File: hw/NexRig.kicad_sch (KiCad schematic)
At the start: 7 parts

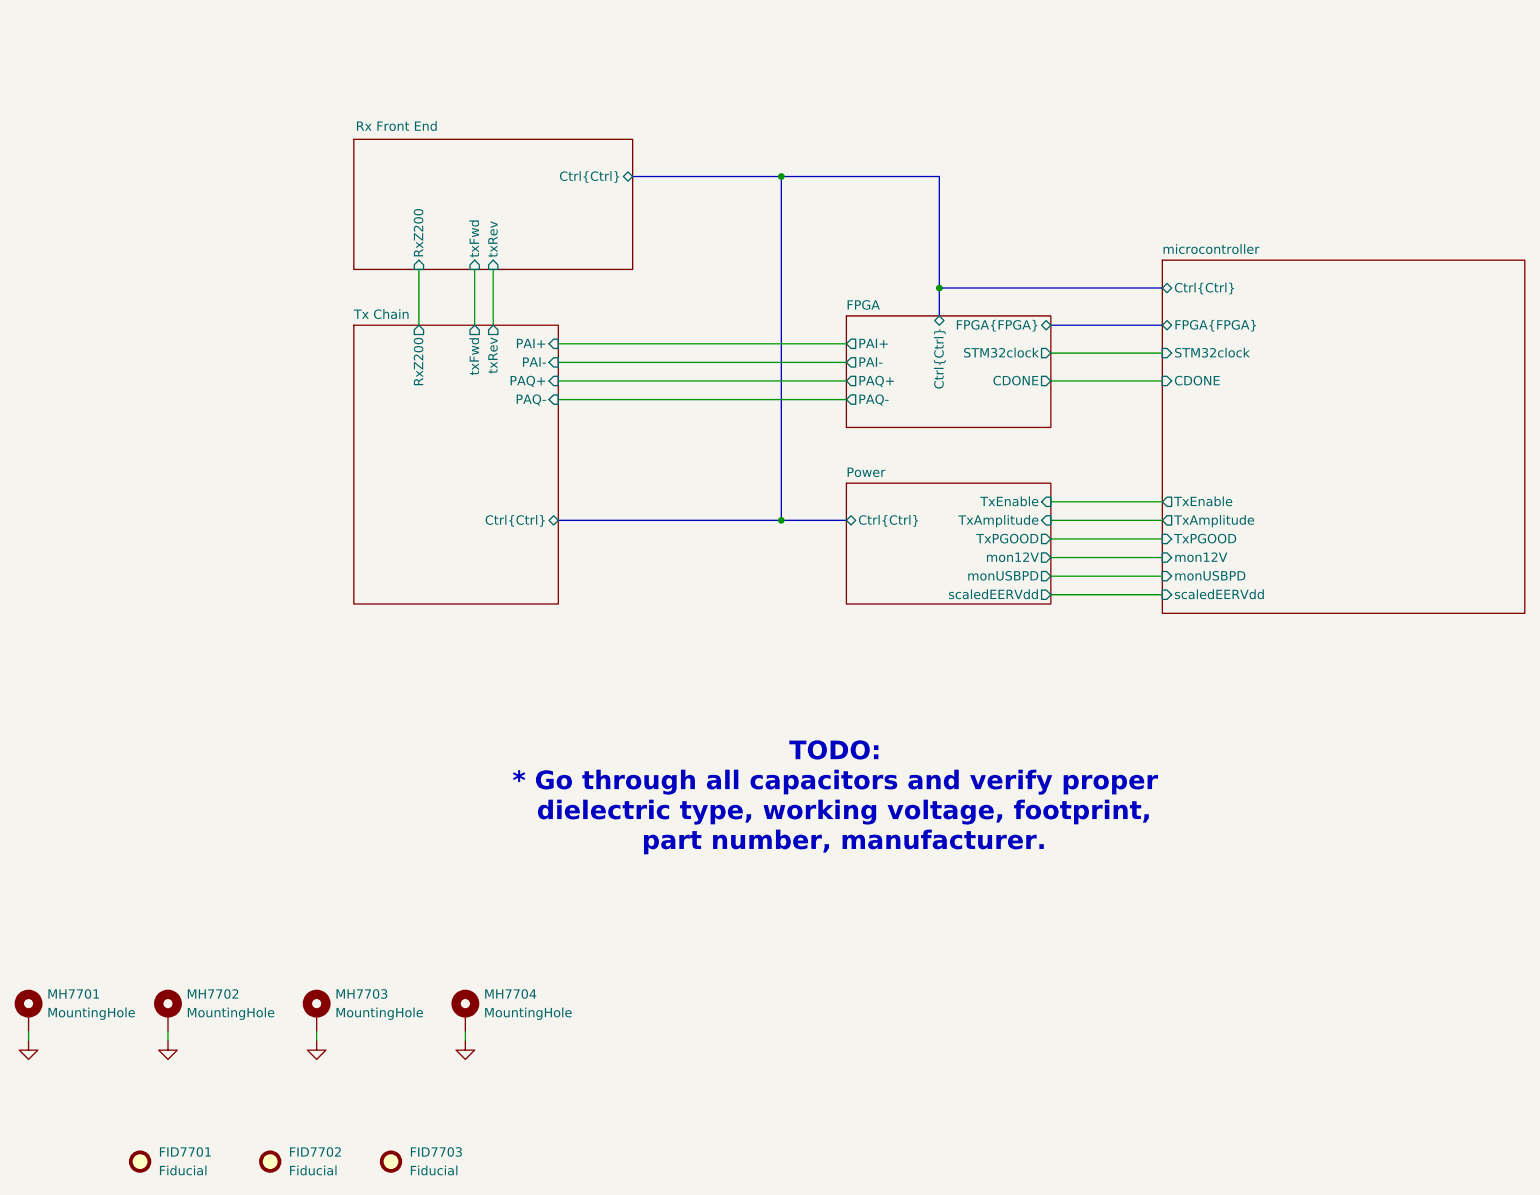
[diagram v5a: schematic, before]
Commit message: Checkpoint. FPGA is mostly done (need a check!). Working on new LPFs. Need inductor footprints and to fix a bunch of broken/missing footprints.
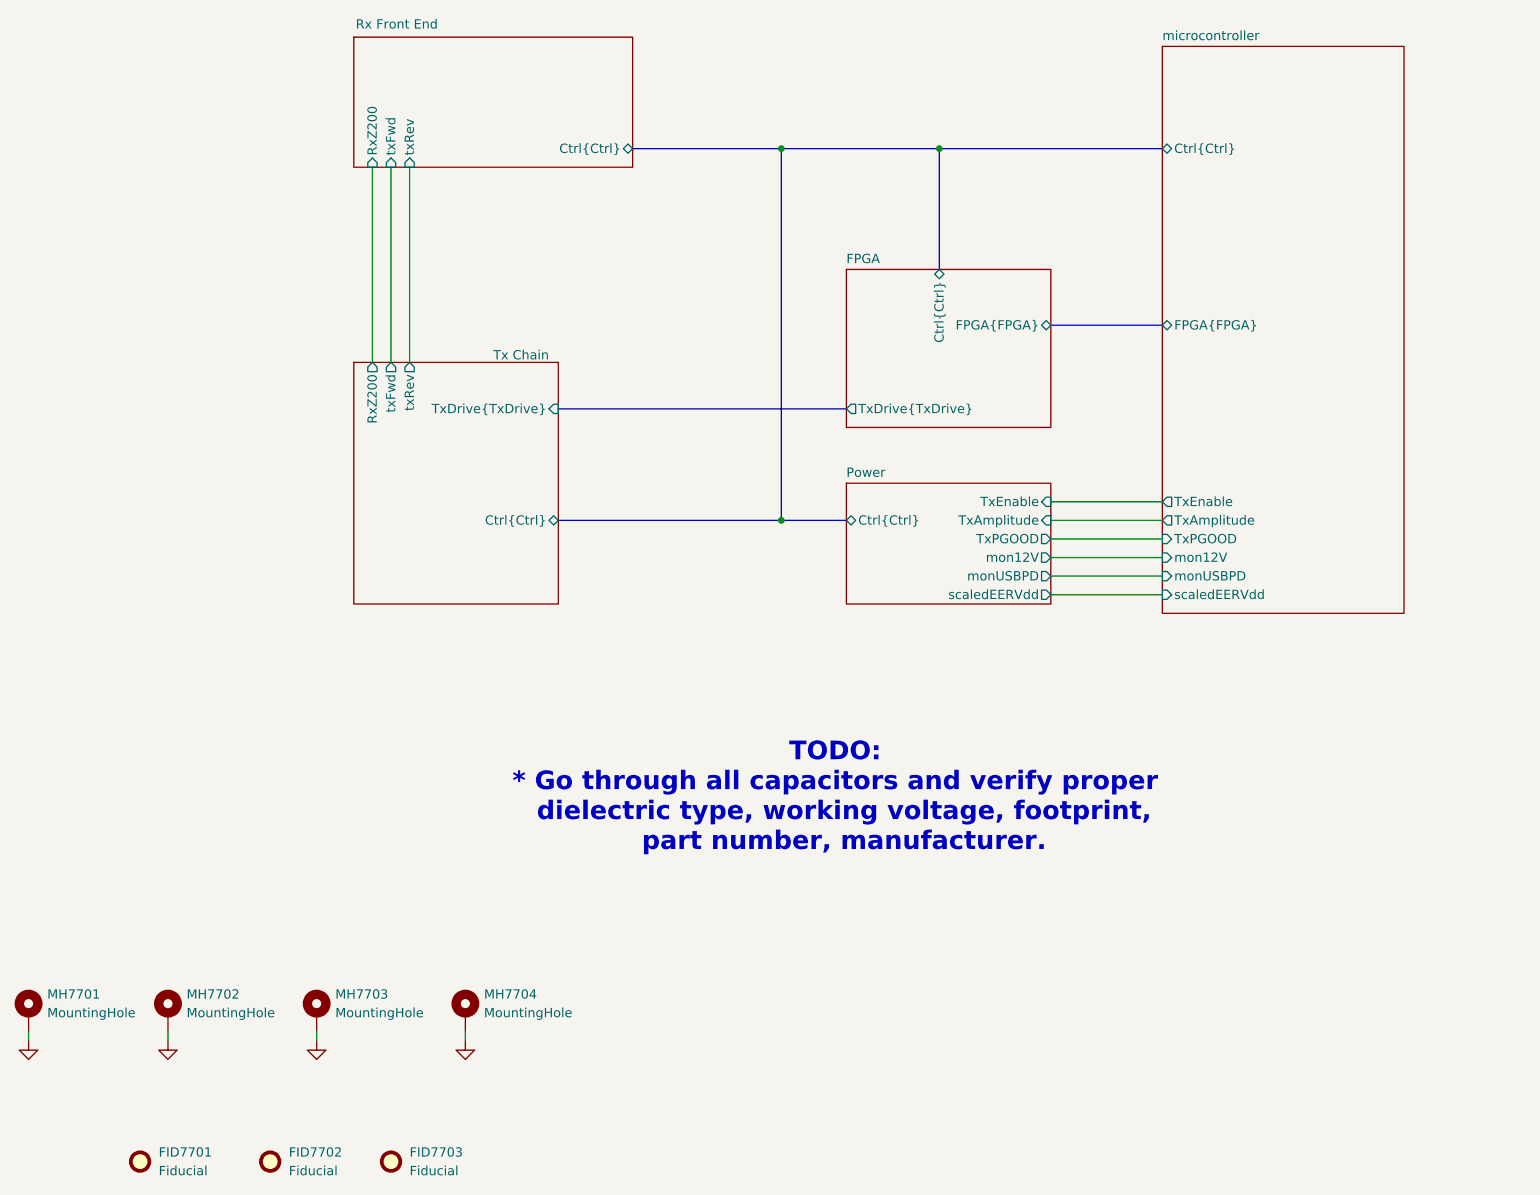
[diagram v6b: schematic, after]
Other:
- sheet FPGA ports: added TxDrive{TxDrive}; removed CDONE, PAI+, PAI-, PAQ+, PAQ-, STM32clock
- sheet Tx Chain ports: added TxDrive{TxDrive}; removed PAI+, PAI-, PAQ+, PAQ-
- sheet microcontroller ports: added none; removed CDONE, STM32clock
